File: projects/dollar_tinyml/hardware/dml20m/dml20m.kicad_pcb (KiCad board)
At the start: 2 copper layers, 52 x 26 mm, 34 parts, among them J2 USB_A, J4 Header 2.54mm, SW1 SW_Push, U1 PY32F003F16P6TU, U2 LP4054HB5F, U3 BM7161, U4 XC6206PxxxMR, U6 LIS2DH12

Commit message: dollarml: Some tweaks
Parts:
- removed D1: CLEAR WHITE, LED_SMD:LED_0603_1608Metric
- removed D2: CLEAR BLUE, LED_SMD:LED_0603_1608Metric
- removed D7: CLEAR GREEN, LED_SMD:LED_0603_1608Metric
- removed D8: CLEAR RED, LED_SMD:LED_0603_1608Metric
- removed R1: 82R, Resistor_SMD:R_0603_1608Metric
- removed REF**: LED_RGB_5050-6, LED_SMD:LED_RGB_5050-6
- added BT1: Battery_Cell, dml20m:Battery_CR1220-Horizontal, F.Cu at (111.7, 100.1)
- added D3: LED_RGB, LED_SMD:LED_RGB_5050-6, F.Cu at (104.3, 106.8)
- added J1: Header 2.54mm, Connector_JST:JST_SH_SM04B-SRSS-TB_1x04-1MP_P1.00mm_Horizontal, B.Cu at (116.9, 93.2)
- added J3: Conn_ARM_SWD_TagConnect_TC2030-NL, Connector:Tag-Connect_TC2030-IDC-NL_2x03_P1.27mm_Vertical, F.Cu at (101.8, 100.2)
- J4: footprint Connector_PinHeader_2.54mm:PinHeader_1x14_P2.54mm_Vertical -> Connector_JST:JST_SH_SM04B-SRSS-TB_1x04-1MP_P1.00mm_Horizontal; moved to B.Cu
- moved R13 40.7 mm to (109.5, 106.1), turned to 90 degrees
- moved J4 27.7 mm to (104.5, 93.0), turned to 180 degrees
- moved R2 25.8 mm to (109.7, 108.6)
- moved R3 25.6 mm to (109.7, 103.7)
- moved TP5 10.8 mm to (107.3, 100.3)
- moved TP6 8.81 mm to (108.7, 103.3)
- moved TP2 7.70 mm to (104.7, 100.9)
- moved TP3 7.27 mm to (109.2, 97.2)
- moved TP7 7.09 mm to (111.1, 102.1)
- moved TP4 6.87 mm to (110.0, 99.8)
- moved C9 1.75 mm to (105.5, 96.9)
- moved U1 1.75 mm to (106.4, 100.0)
- moved U4 0.61 mm to (108.7, 92.2)
- moved H1 0.47 mm to (99.4, 96.7)
- moved SW1 0.42 mm to (123.9, 106.8)
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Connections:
- J4 pad 1: unconnected-(J4-Pin_1-Pad1) -> /BOOT0
- J4 pad 4: /SCL -> unconnected-(J4-Pin_4-Pad4)
- U1 pad 14: /LED_WHITE_N -> unconnected-(U1-PB7-Pad14)
- U1 pad 19: /AUDIO_LOW -> unconnected-(U1-PA0-Pad19)
- U1 pad 20: /AUDIO_HIGH -> unconnected-(U1-PA1-Pad20)
- U1 pad 8: /MIC_POWER_CTRL -> unconnected-(U1-PA12-Pad8)
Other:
- board size 52 x 26 mm -> 39.9 x 19.8 mm

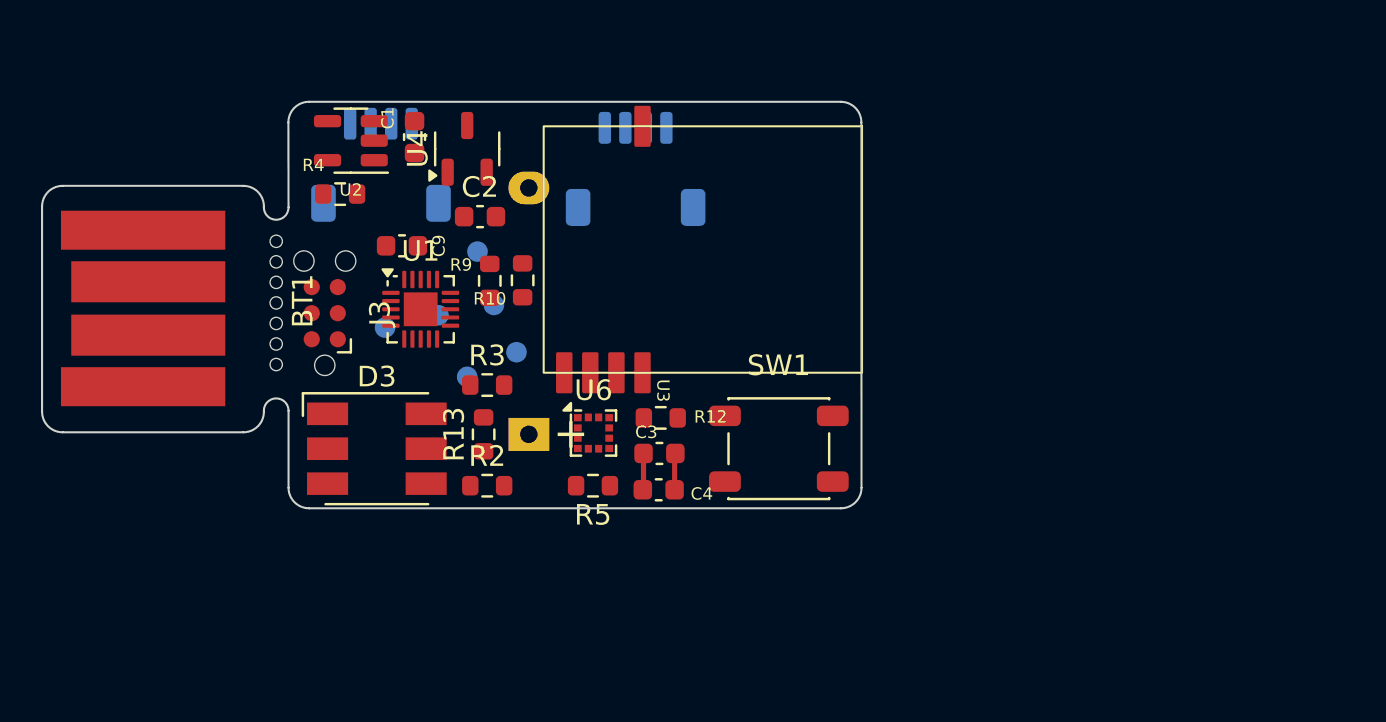
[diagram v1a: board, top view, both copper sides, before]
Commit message: dollarml: Almost everything routed
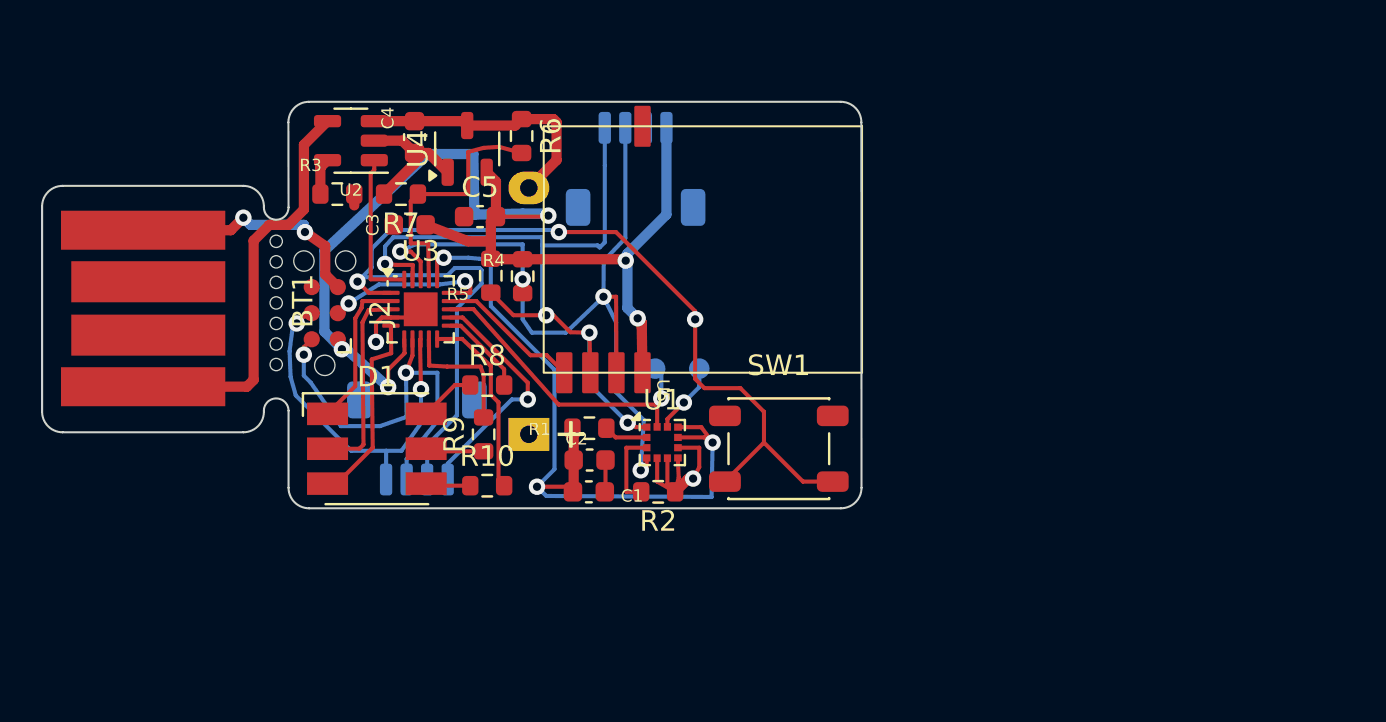
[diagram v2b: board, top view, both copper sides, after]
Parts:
- removed the TP2 at (104.7, 100.9)
- removed TP3, TP4, TP7: TP_PCB, TestPoint:TestPoint_Pad_D1.0mm
- added R6: 10k, Resistor_SMD:R_0603_1608Metric, F.Cu at (111.3, 91.6)
- added R7: 10k, Resistor_SMD:R_0603_1608Metric, F.Cu at (105.5, 94.4)
- U3: renamed from U1; value PY32F003F16P6TU -> PY32F003F18U6TR
- moved J3 13.4 mm to (106.2, 106.3), turned to 0 degrees
- moved TP2 11.3 mm to (120.0, 102.9)
- moved TP1 10.9 mm to (117.8, 102.9)
- moved R1 3.51 mm to (114.7, 105.8), turned to 180 degrees
- moved C2 3.42 mm to (114.7, 107.3)
- moved C1 3.40 mm to (114.6, 108.9)
- moved U1 3.38 mm to (118.2, 106.5)
- moved R2 3.19 mm to (118.0, 108.9)
- moved R4 1.62 mm to (111.4, 98.4)
- moved R5 1.57 mm to (109.8, 98.4)
- moved C3 1.09 mm to (105.9, 95.9), turned to 0 degrees
- moved R3 0.14 mm to (102.4, 94.4)
- renumbered C4 to C1, C3 to C2, C9 to C3, C1 to C4, C2 to C5, D3 to D1, J2 to J1, J3 to J2, J4 to J3, J1 to J4, R12 to R1, R2 to R10, R5 to R2, R4 to R3, R9 to R4, R10 to R5, R3 to R8, R13 to R9, TP5 to TP1, TP6 to TP2, U6 to U1, U3 to U5
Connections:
- J3 pad 1: /BOOT0 -> /SWCLK
- J3 pad 2: unconnected-(J4-Pin_2-Pad2) -> /SWDIO
- J3 pad 3: unconnected-(J4-Pin_3-Pad3) -> /BUTTON_1
- J3 pad 4: unconnected-(J4-Pin_4-Pad4) -> /BOOT0
- J4 pad 2: /SCL -> GND
- J4 pad 4: GND -> /SCL
- U2 pad 1: /CHRG -> /BATT_CHRG
- U3 pad 1: /SDA -> /BUTTON_1
- U3 pad 10: /SWDIO -> /LED_BLUE_N
- U3 pad 11: /SWCLK -> /LED_GREEN_N
- U3 pad 12: /LED_BLUE_P -> /BOOT0
- U3 pad 13: /LED_BLUE_N -> /ACC_INT1
- U3 pad 14: unconnected-(U1-PB7-Pad14) -> /BLE_INT
- U3 pad 15: /BOOT0 -> /RESET
- U3 pad 16: /LED_GREEN_P -> /ACC_POWER
- U3 pad 17: /LED_GREEN_N -> /BATT_VOLTAGE
- U3 pad 18: /RESET -> /SDA
- U3 pad 19: unconnected-(U1-PA0-Pad19) -> /SCL
- U3 pad 2: /SCL -> /LED_GREEN_P
- U3 pad 20: unconnected-(U1-PA1-Pad20) -> /BATT_CHRG
- U3 pad 21: (no net) -> GND
- U3 pad 3: /BLE_INT -> /LED_RED_P
- U3 pad 4: /ACC_INT1 -> GND
- U3 pad 5: /LED_RED_P -> /LED_BLUE_P
- U3 pad 6: /LED_RED_N -> VDD
- U3 pad 7: GND -> /SWDIO
- U3 pad 8: unconnected-(U1-PA12-Pad8) -> /SWCLK
- U3 pad 9: VDD -> /LED_RED_N
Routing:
- net VDD: track 0.00 -> 57.2 mm, vias 0 -> 5
- net /BUTTON_1: track 0.00 -> 54.8 mm, vias 0 -> 3
- net /SDA: track 0.00 -> 40.4 mm, vias 0 -> 4
- net /SCL: track 0.00 -> 37.6 mm, vias 0 -> 4
- net /ACC_POWER: track 1.73 -> 36.4 mm, vias 0 -> 3
- net GND: track 1.73 -> 33.7 mm, vias 0 -> 4
- net VBUS: track 0.00 -> 20.2 mm
- net /SWDIO: track 0.00 -> 19.4 mm, vias 0 -> 2
- net /SWCLK: track 0.00 -> 18.3 mm, vias 0 -> 2
- net /ACC_INT1: track 0.00 -> 15.5 mm, vias 0 -> 1
- net /BATT+: track 0.00 -> 12.9 mm
- net /BATT_VOLTAGE: track 0.00 -> 12.3 mm
- net /BOOT0: track 0.00 -> 11.9 mm, vias 0 -> 1
- net /LED_BLUE_P: track 0.00 -> 9.56 mm
- net /LED_RED_P: track 0.00 -> 9.54 mm
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
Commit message: dollarml: Layout of rev2 for motion done
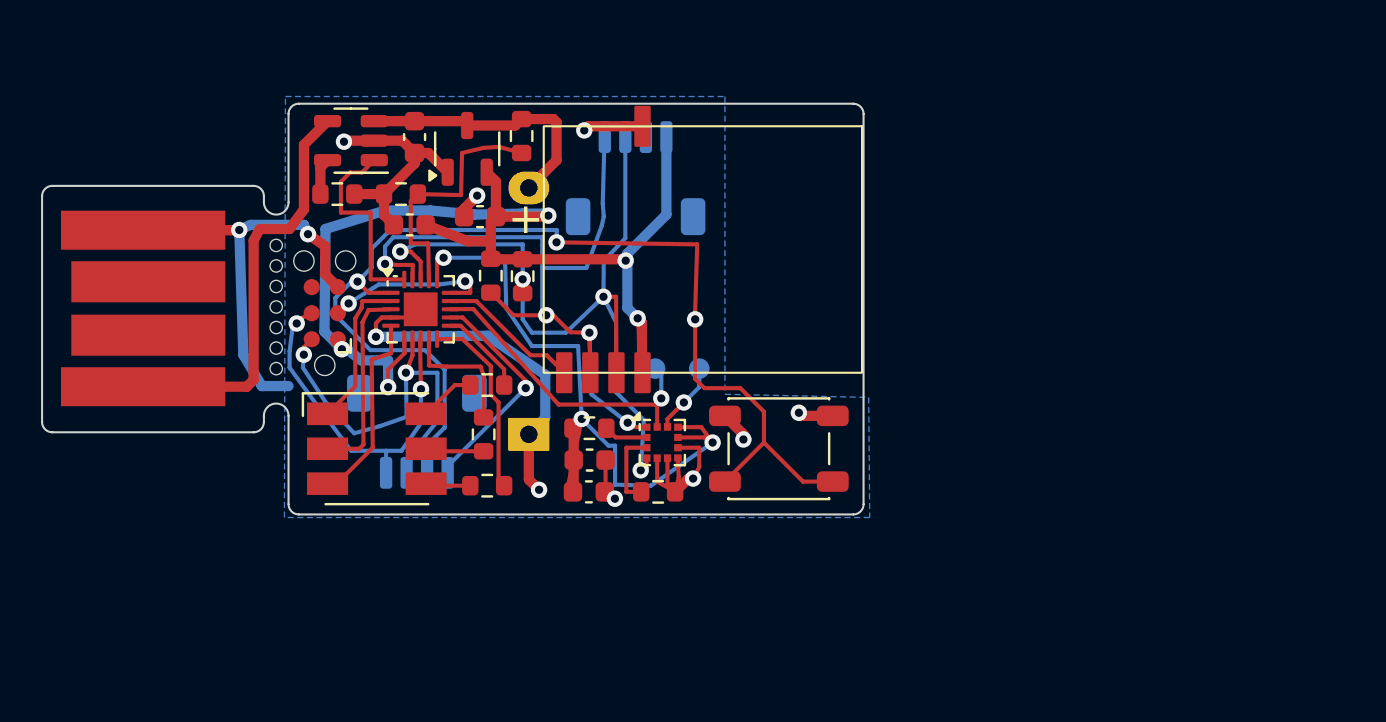
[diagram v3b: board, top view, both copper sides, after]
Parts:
- moved J4 0.45 mm to (116.9, 93.6)
- moved J3 0.33 mm to (106.2, 106.0)
- moved H1 0.20 mm to (99.4, 96.9)
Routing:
- net GND: track 33.7 -> 70.1 mm, vias 4 -> 11
- net VDD: track 57.2 -> 54.3 mm
- net /BATT_CHRG: track 7.51 -> 9.89 mm
- net /ACC_POWER: track 36.4 -> 34.8 mm
- net /BUTTON_1: track 54.8 -> 53.8 mm
- added copper zone on B.Cu, net GND
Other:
- board size 39.9 x 19.8 mm -> 40 x 20 mm

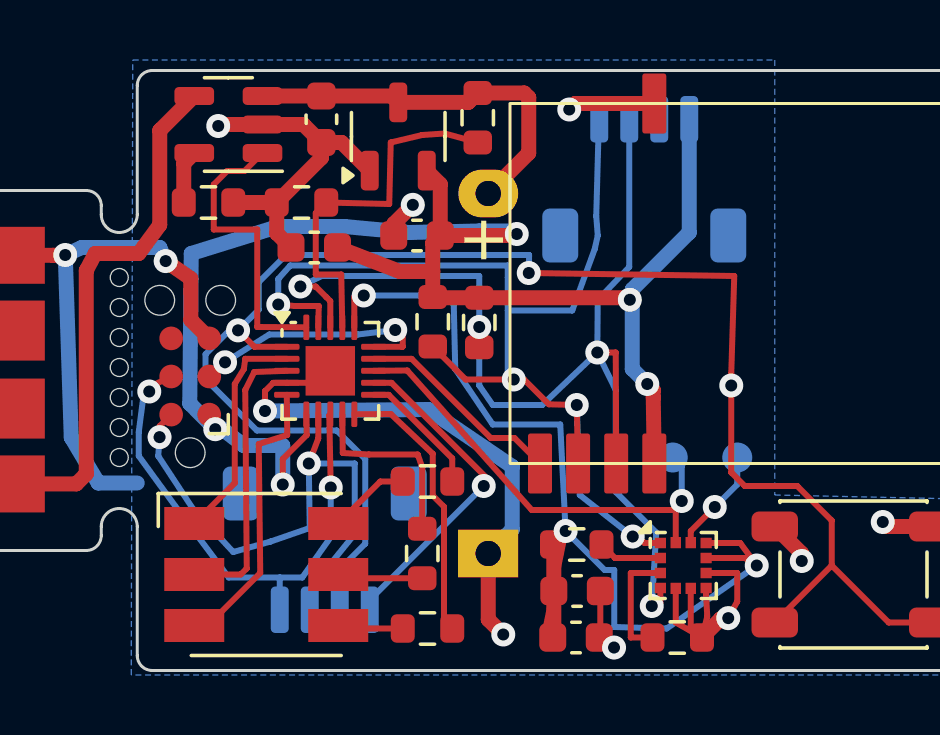
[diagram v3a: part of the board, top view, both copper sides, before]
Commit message: dollarml: Split I2C to BLE, add buzzer
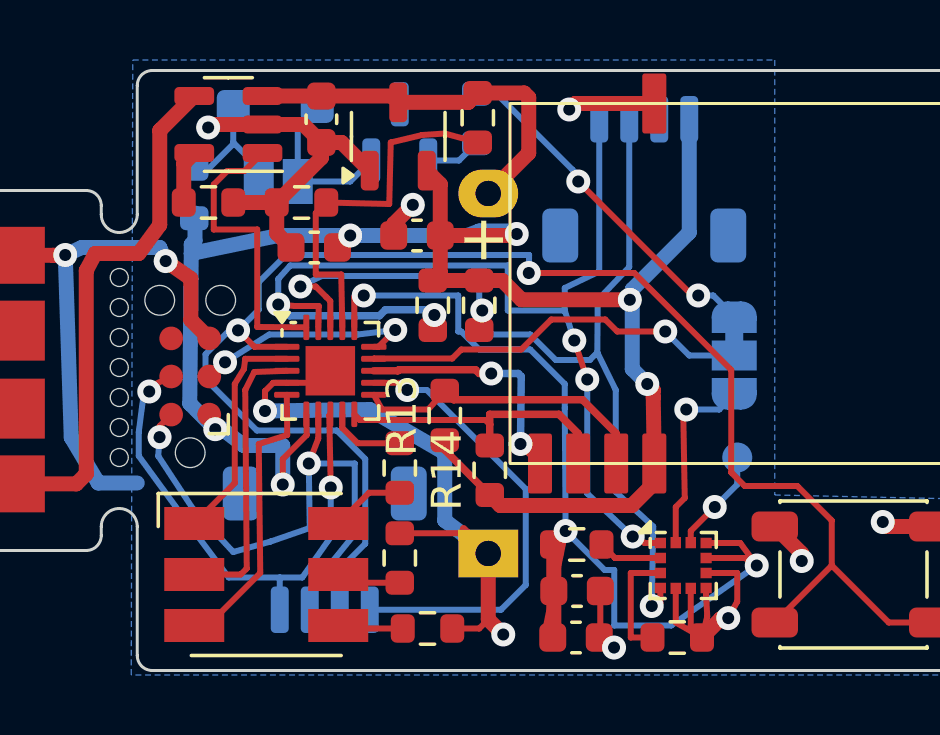
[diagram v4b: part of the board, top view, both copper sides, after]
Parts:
- removed TP1: TP_PCB, TestPoint:TestPoint_Pad_D1.0mm
- added BZ1: Buzzer, Jumper:SolderJumper-2_P1.3mm_Open_Pad1.0x1.5mm, B.Cu at (104.7, 93.7)
- added D2: 1N4001, Diode_SMD:D_SOD-123F, B.Cu at (104.6, 91.2)
- added JP1: SolderJumper_3_Bridged12, Jumper:SolderJumper-3_P1.3mm_Bridged12_RoundedPad1.0x1.5mm, B.Cu at (119.9, 99.5)
- added Q1: BC547B, Package_TO_SOT_SMD:SOT-23, B.Cu at (108.8, 92.1)
- added R11: 100R, Resistor_SMD:R_0603_1608Metric, B.Cu at (111.3, 91.6)
- added R12: 33R, Resistor_SMD:R_0603_1608Metric, B.Cu at (101.9, 94.1)
- added R13: 3.3k, Resistor_SMD:R_0603_1608Metric, F.Cu at (110.2, 101.5)
- added R14: 3.3k, Resistor_SMD:R_0603_1608Metric, F.Cu at (111.8, 103.3)
- moved R8 1.03 mm to (108.8, 103.2), turned to 90 degrees
- moved R9 0.76 mm to (108.8, 106.2)
- moved R4 0.58 mm to (111.4, 97.8)
- moved R5 0.55 mm to (109.8, 97.8)
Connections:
- R10 pad 2: /LED_BLUE_N -> GND
- R9 pad 2: /LED_RED_N -> GND
- U3 pad 10: /LED_BLUE_N -> /BLE_SCL
- U3 pad 11: /LED_GREEN_N -> /BLE_SDA
- U3 pad 13: /ACC_INT1 -> /BLE_INT
- U3 pad 14: /BLE_INT -> /ACC_INT/BUZZER
- U3 pad 9: /LED_RED_N -> /LED_GREEN_N
- U5 pad 2: /SCL -> /BLE_SCL
- U5 pad 3: /SDA -> /BLE_SDA
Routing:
- net /ACC_INT/BUZZER: track 0.00 -> 13.1 mm, vias 0 -> 1
- net /BUZZER: track 0.00 -> 11.8 mm, vias 0 -> 2
- net /BLE_SCL: track 0.00 -> 10.3 mm
- net /BLE_SDA: track 0.00 -> 10.2 mm
- net /LED_BLUE_N: track 9.24 -> 0.00 mm
- net /ACC_INT1: track 15.5 -> 6.41 mm
- net VDD: track 54.3 -> 61.8 mm, vias 5 -> 6
- net /SDA: track 40.4 -> 33.7 mm, vias 4 -> 3
- net /LED_RED_N: track 6.29 -> 0.00 mm
- net Net-(BZ1--): track 0.00 -> 5.51 mm
- net GND: track 70.1 -> 74.9 mm
- net Net-(BZ1-+): track 0.00 -> 4.54 mm
- net /BOOT0: track 11.8 -> 16.4 mm
- net /BUTTON_1: track 53.8 -> 51.9 mm, vias 3 -> 2
- net Net-(Q1-B): track 0.00 -> 1.84 mm
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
